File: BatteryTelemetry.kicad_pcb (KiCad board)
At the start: 2 copper layers, 137 parts, among them IC1 BQ76925PWR, IC2 BQ76925PWR, IC3 BQ76925PWR, IC4 BQ76925PWR, J1 Conn_01x07_Pin, J2 Conn_01x07_Pin, J3 Conn_01x07_Pin, J4 Conn_01x07_Pin, J5 USB_C_Receptacle_USB2.0, J6 Conn_01x04_Socket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

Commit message: Layout Complete
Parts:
- C37: footprint Capacitor_SMD:C_0805_2012Metric -> Capacitor_SMD:C_0805_2012Metric_Pad1.18x1.45mm_HandSolder
- H1, H2, H3, H4: footprint MountingHole:MountingHole_3.2mm_M3 -> MountingHole:MountingHole_3.2mm_M3_DIN965_Pad
- moved H3 100.7 mm to (30.0, 155.0)
- moved C36 97.4 mm to (64.0, 136.7)
- moved H1 93.6 mm to (30.0, 30.0)
- moved C46 85.7 mm to (61.5, 122.3)
- moved C45 83.5 mm to (62.6, 127.4), turned to 180 degrees
- moved C47 81.4 mm to (62.6, 129.4), turned to 180 degrees
- moved C44 79.5 mm to (62.6, 125.3), turned to 180 degrees
- moved R52 78.8 mm to (64.0, 141.4)
- moved H4 73.7 mm to (75.0, 155.0)
- moved H2 72.1 mm to (75.0, 30.0)
- moved SW2 66.0 mm to (71.8, 140.4)
- moved SW1 64.5 mm to (71.8, 146.0)
- moved J7 60.7 mm to (77.1, 111.8), turned to 180 degrees
- moved R51 60.1 mm to (55.6, 146.0), turned to 180 degrees
- moved R50 59.7 mm to (59.9, 146.0), turned to 180 degrees
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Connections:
- SW3 pad 4: (no net) -> /V3_BAT
- SW3 pad 5: (no net) -> Net-(D6-A)
- SW3 pad 6: (no net) -> /V3_EXT
- U4 pad 10: /SDA_BAT3 -> /SDA_BAT4
- U4 pad 11: /SCL_BAT3 -> /SCL_BAT4
- U4 pad 13: /SDA_BAT4 -> unconnected-(U4-SD4-Pad13)
- U4 pad 14: /SCL_BAT4 -> unconnected-(U4-SC4-Pad14)
- U4 pad 4: unconnected-(U4-SD0-Pad4) -> /SDA_BAT1
- U4 pad 5: unconnected-(U4-SC0-Pad5) -> /SCL_BAT1
- U4 pad 6: /SDA_BAT1 -> /SDA_BAT2
- U4 pad 7: /SCL_BAT1 -> /SCL_BAT2
- U4 pad 8: /SDA_BAT2 -> /SDA_BAT3
- U4 pad 9: /SCL_BAT2 -> /SCL_BAT3
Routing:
- net GND: track 0.00 -> 353.9 mm, vias 0 -> 36
- net +3V3: track 136.7 -> 222.7 mm, vias 4 -> 8
- net /RESET: track 5.75 -> 53.6 mm, vias 0 -> 3
- net /BAT1: track 37.5 -> 85.0 mm
- net /SDA_BAT4: track 15.6 -> 56.8 mm, vias 2 -> 0
- net /BAT2: track 15.8 -> 55.9 mm, vias 2 -> 0
- net /SCL_BAT4: track 18.0 -> 57.0 mm
- net /RUN: track 4.41 -> 39.9 mm, vias 0 -> 1
- net /USB_D+: track 11.8 -> 47.1 mm, vias 1 -> 0
- net /USB_D-: track 13.1 -> 44.7 mm
- net /I2C0 SDA: track 7.40 -> 36.1 mm
- net /SDA_BAT2: track 12.8 -> 37.4 mm
- net /I2C0 SCL: track 9.73 -> 32.6 mm
- net /BAT3: track 38.4 -> 18.4 mm, vias 2 -> 0
- net /SCL_BAT3: track 35.1 -> 17.2 mm
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- added copper zone on B.Cu, net GND
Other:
- board outline added: 55 x 135 mm
- board text added: "BAT Power"
- board text added: "CTS"
- board text added: "EXT"
- board text added: "GND"
- board text added: "Input Power"
- board text added: "RTS"
- board text added: "RX"
- board text added: "SWCLK"
- board text added: "SWD"
- board text added: "SWD Debug Breakout"
- board text added: "TX"
- board text added: "UART Breakout"
- board text added: "V3"
- board text added: "V5 (or)"

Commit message: Updated Layout
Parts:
- added TP1: TestPoint, TestPoint:TestPoint_THTPad_D1.5mm_Drill0.7mm, F.Cu at (52.5, 28.3)
- added TP10: TestPoint, TestPoint:TestPoint_THTPad_D1.5mm_Drill0.7mm, F.Cu at (33.0, 124.7)
- added TP11: TestPoint, TestPoint:TestPoint_THTPad_D1.5mm_Drill0.7mm, F.Cu at (53.2, 63.9)
- added TP12: TestPoint, TestPoint:TestPoint_THTPad_D1.5mm_Drill0.7mm, F.Cu at (53.5, 121.8)
- added TP13: TestPoint, TestPoint:TestPoint_THTPad_D1.5mm_Drill0.7mm, F.Cu at (77.1, 78.0)
- added TP14: TestPoint, TestPoint:TestPoint_THTPad_D1.5mm_Drill0.7mm, F.Cu at (77.1, 81.5)
- added TP15: TestPoint, TestPoint:TestPoint_THTPad_D1.5mm_Drill0.7mm, F.Cu at (77.1, 85.1)
- added TP2: TestPoint, TestPoint:TestPoint_THTPad_D1.5mm_Drill0.7mm, F.Cu at (55.7, 28.3)
- added TP3: TestPoint, TestPoint:TestPoint_THTPad_D1.5mm_Drill0.7mm, F.Cu at (58.9, 28.3)
- added TP4: TestPoint, TestPoint:TestPoint_THTPad_D1.5mm_Drill0.7mm, F.Cu at (62.1, 28.3)
- added TP5: TestPoint, TestPoint:TestPoint_THTPad_D1.5mm_Drill0.7mm, F.Cu at (65.3, 28.3)
- added TP6: TestPoint, TestPoint:TestPoint_THTPad_D1.5mm_Drill0.7mm, F.Cu at (68.5, 28.3)
- added TP7: TestPoint, TestPoint:TestPoint_THTPad_D1.5mm_Drill0.7mm, F.Cu at (33.0, 61.4)
- added TP8: TestPoint, TestPoint:TestPoint_THTPad_D1.5mm_Drill0.7mm, F.Cu at (33.0, 65.0)
- added TP9: TestPoint, TestPoint:TestPoint_THTPad_D1.5mm_Drill0.7mm, F.Cu at (33.0, 121.2)
- moved C29 12.8 mm to (64.5, 46.4), turned to -90 degrees
- moved D5 3.44 mm to (69.5, 46.4)
- moved C37 2.69 mm to (69.5, 70.0)
- moved C38 2.69 mm to (69.5, 72.5)
- moved C39 2.69 mm to (69.5, 75.0)
- moved C40 2.69 mm to (69.5, 77.5)
- moved C41 2.69 mm to (69.5, 80.0)
- moved C42 2.69 mm to (69.5, 82.5)
- moved C43 2.69 mm to (69.5, 85.0)
- moved D6 2.26 mm to (67.0, 46.4)
- moved SW3 2.23 mm to (64.5, 38.9)
- moved SW1 0.93 mm to (71.9, 146.9)
- moved SW2 0.83 mm to (71.9, 139.6)
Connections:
- H1 pad 1: (no net) -> /Chassis
- H2 pad 1: (no net) -> /Chassis
- H3 pad 1: (no net) -> /Chassis
- H4 pad 1: (no net) -> /Chassis
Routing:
- net /Chassis: track 0.00 -> 217.3 mm
- net GND: track 353.9 -> 243.5 mm, vias 36 -> 37
- net /SCL_BAT3: track 17.2 -> 61.6 mm, vias 0 -> 1
- net /SDA_BAT3: track 20.0 -> 63.4 mm, vias 0 -> 1
- net /V3_USB: track 13.1 -> 44.9 mm, vias 0 -> 1
- net +3V3: track 222.7 -> 253.9 mm
- net /SDA_BAT1: track 49.3 -> 78.9 mm, vias 0 -> 1
- net /SCL_BAT1: track 52.1 -> 77.5 mm, vias 0 -> 1
- net /RESET: track 53.6 -> 73.2 mm
- net Net-(D4-K): track 21.9 -> 41.2 mm, vias 0 -> 1
- net /I2C0 SDA: track 36.1 -> 54.9 mm, vias 0 -> 1
- net /I2C0 SCL: track 32.6 -> 50.9 mm, vias 0 -> 1
- net Net-(D6-A): track 5.75 -> 21.9 mm
- net /V3_EXT: track 8.60 -> 24.5 mm
- net /V3_BAT: track 21.0 -> 32.3 mm
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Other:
- board text added: "(V3_EXT)"
- board text added: "Antonio Molteni"
- board text added: "BOOT"
- board text added: "Battery Telemetry Module"
- board text added: "Designed and Built by"
- board text added: "EXT Power"
- board text added: "RESET"
- board text added: "TP1"
- board text added: "TP2"
- board text added: "TP3"
- board text added: "TP4"
- board text added: "TP5"
- board text added: "TP6"
- board text added: "UAVs@Berkeley"
- board text added: "V5"
- board text added: "Yihui Liang"
- board text removed: "EXT"

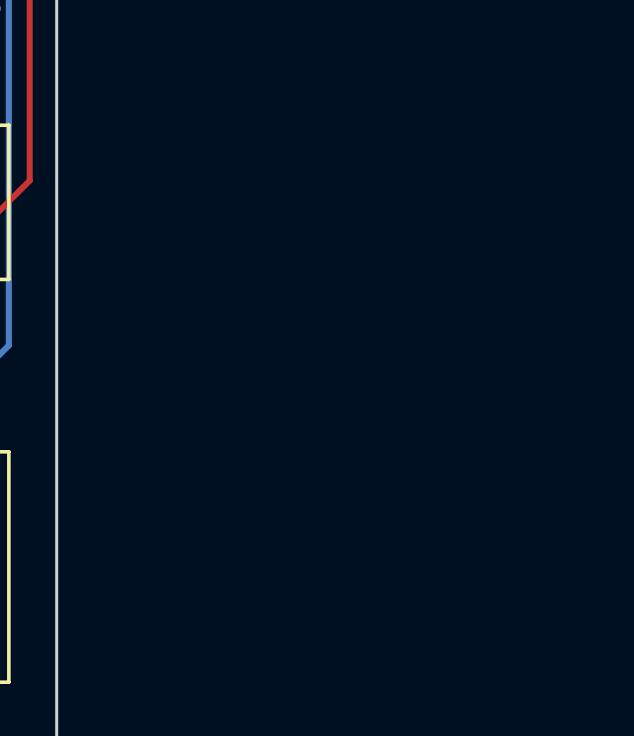
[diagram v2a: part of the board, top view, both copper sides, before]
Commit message: RC circuit for VCout
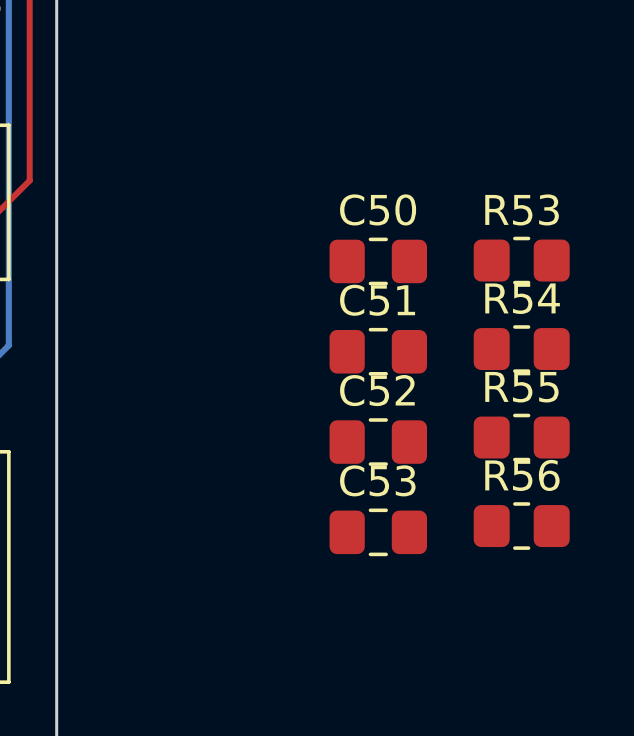
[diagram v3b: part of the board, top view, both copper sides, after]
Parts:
- added C50: 0.1uF, Capacitor_SMD:C_0805_2012Metric_Pad1.18x1.45mm_HandSolder, F.Cu at (90.7, 110.0)
- added C51: 0.1uF, Capacitor_SMD:C_0805_2012Metric_Pad1.18x1.45mm_HandSolder, F.Cu at (90.7, 113.0)
- added C52: 0.1uF, Capacitor_SMD:C_0805_2012Metric_Pad1.18x1.45mm_HandSolder, F.Cu at (90.7, 116.0)
- added C53: 0.1uF, Capacitor_SMD:C_0805_2012Metric_Pad1.18x1.45mm_HandSolder, F.Cu at (90.7, 119.0)
- added R53: 0, Resistor_SMD:R_0805_2012Metric_Pad1.20x1.40mm_HandSolder, F.Cu at (95.5, 110.0)
- added R54: 0, Resistor_SMD:R_0805_2012Metric_Pad1.20x1.40mm_HandSolder, F.Cu at (95.5, 112.9)
- added R55: 0, Resistor_SMD:R_0805_2012Metric_Pad1.20x1.40mm_HandSolder, F.Cu at (95.5, 115.8)
- added R56: 0, Resistor_SMD:R_0805_2012Metric_Pad1.20x1.40mm_HandSolder, F.Cu at (95.5, 118.8)
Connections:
- U1 pad 38: /BAT1 -> Net-(U1-GPIO26_ADC0)
- U1 pad 39: /BAT2 -> Net-(U1-GPIO27_ADC1)
- U1 pad 40: /BAT3 -> Net-(U1-GPIO28_ADC2)
- U1 pad 41: /BAT4 -> Net-(U1-GPIO29_ADC3)

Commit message: RC for Vcout Layout Updated
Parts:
- moved R53 55.4 mm to (57.6, 69.5), turned to 90 degrees
- moved C50 52.6 mm to (59.7, 67.5), turned to -90 degrees
- moved C51 42.5 mm to (64.3, 79.7)
- moved C52 36.1 mm to (56.1, 126.3), turned to -90 degrees
- moved R56 36.0 mm to (63.2, 134.7), turned to -90 degrees
- moved R55 34.1 mm to (61.5, 117.7), turned to 90 degrees
- moved R54 31.8 mm to (67.6, 97.6), turned to 90 degrees
- moved C53 30.8 mm to (62.6, 131.6), turned to 180 degrees
- moved C36 9.58 mm to (66.2, 146.0), turned to 0 degrees
- moved R52 1.18 mm to (65.2, 141.4)
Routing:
- net /BAT1: track 90.3 -> 29.0 mm
- net Net-(U1-GPIO26_ADC0): track 0.00 -> 60.8 mm, vias 0 -> 2
- net Net-(U1-GPIO27_ADC1): track 0.00 -> 28.0 mm
- net /BAT2: track 55.9 -> 30.6 mm
- net GND: track 243.5 -> 264.0 mm, vias 37 -> 40
- net Net-(U1-GPIO29_ADC3): track 0.00 -> 14.8 mm
- net /BAT4: track 20.2 -> 8.60 mm
- net Net-(U1-GPIO28_ADC2): track 0.00 -> 7.68 mm
- net /BAT3: track 28.6 -> 25.5 mm
- net /I2C0 SCL: track 50.9 -> 52.2 mm
- net +3V3: track 253.9 -> 255.1 mm
- net /I2C0 SDA: track 54.9 -> 55.9 mm
